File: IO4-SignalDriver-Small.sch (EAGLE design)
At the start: 17 parts, among them IC1 74HS139A

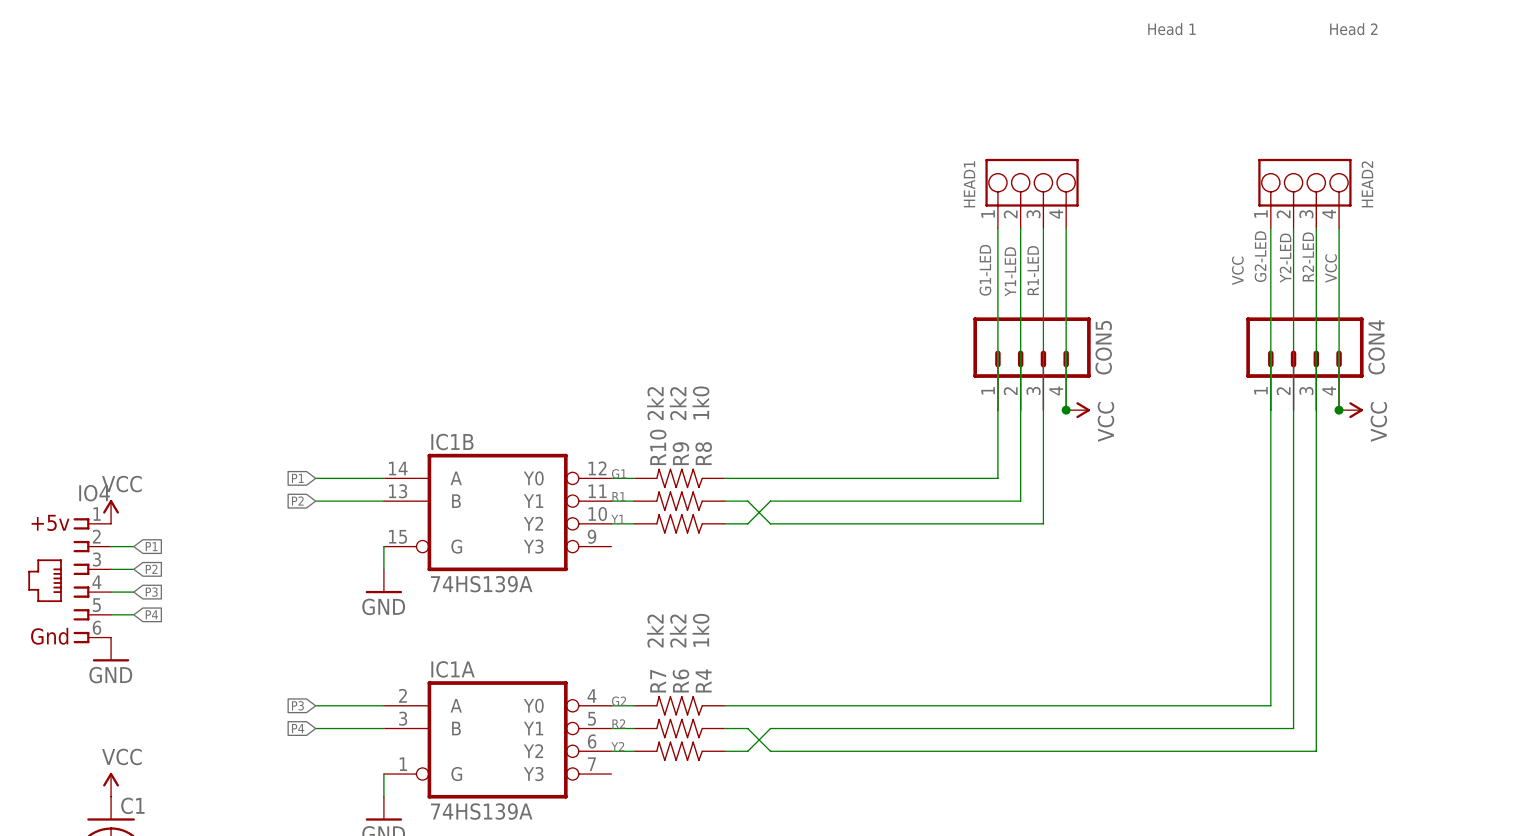
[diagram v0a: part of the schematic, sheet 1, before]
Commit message: added values for connectors
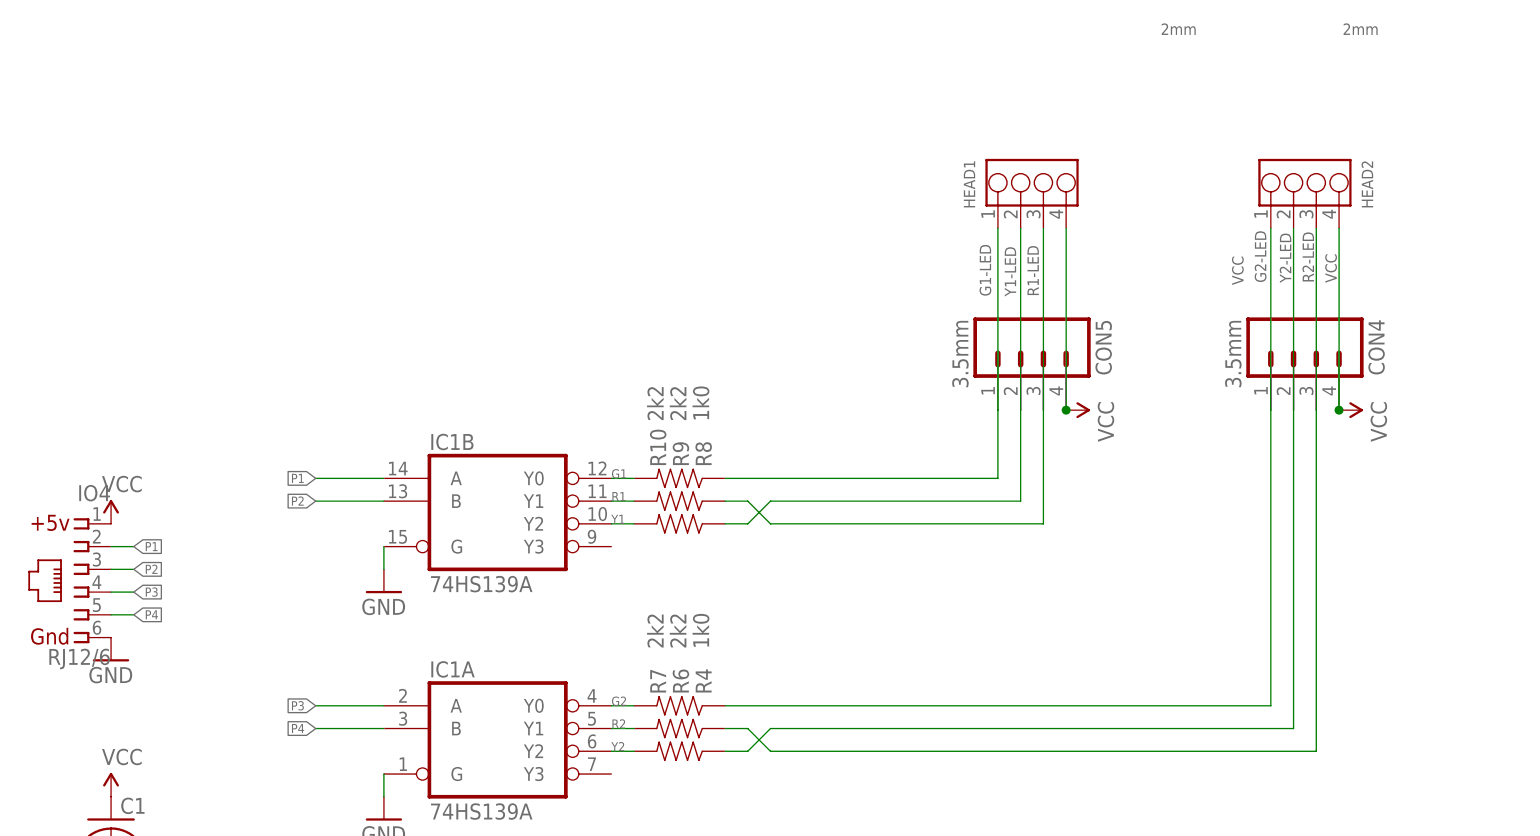
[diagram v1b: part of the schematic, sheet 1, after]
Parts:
- CON4, CON5: value (none) -> 3.5mm
- HEAD1: value Head 1 -> 2mm
- HEAD2: value Head 2 -> 2mm
- IO4: value (none) -> RJ12/6
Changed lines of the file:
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@@
 <grid distance="100" unitdist="mil" unit="mil" style="dots" multiple="1" display="yes" altdistance="50" altunitdist="mil" altunit="mil"/>
 <layers>
-<layer number="1" name="Top" color="4" fill="1" visible="yes" active="no"/>
-<layer number="2" name="Route2" color="1" fill="3" visible="yes" active="no"/>
-<layer number="3" name="Route3" color="4" fill="3" visible="yes" active="no"/>
-<layer number="14" name="Route14" color="1" fill="6" visible="yes" active="no"/>
-<layer number="15" name="Route15" color="4" fill="6" visible="yes" active="no"/>
-<layer number="16" name="Bottom" color="2" fill="1" visible="yes" active="no"/>
-<layer number="17" name="Pads" color="23" fill="1" visible="yes" active="no"/>
-<layer number="18" name="Vias" color="29" fill="1" visible="yes" active="no"/>
-<layer number="19" name="Unrouted" color="6" fill="1" visible="yes" active="no"/>
-<layer number="20" name="Dimension" color="15" fill="1" visible="yes" active="no"/>
-<layer number="21" name="tPlace" color="19" fill="1" visible="yes" active="no"/>
-<layer number="22" name="bPlace" color="17" fill="1" visible="yes" active="no"/>
-<layer number="23" name="tOrigins" color="30" fill="1" visible="yes" active="no"/>
-<layer number="24" name="bOrigins" color="15" fill="1" visible="yes" active="no"/>
-<layer number="25" name="tNames" color="63" fill="1" visible="yes" active="no"/>
-<layer number="26" name="bNames" color="34" fill="1" visible="yes" active="no"/>
-<layer number="27" name="tValues" color="56" fill="1" visible="yes" active="no"/>
-<layer number="28" name="bValues" color="7" fill="1" visible="yes" active="no"/>
+<layer number="1" name="Top" color="4" fill="1" visible="no" active="no"/>
+<layer number="2" name="Route2" color="1" fill="3" visible="no" active="no"/>
+<layer number="3" name="Route3" color="4" fill="3" visible="no" active="no"/>
+<layer number="14" name="Route14" color="1" fill="6" visible="no" active="no"/>
+<layer number="15" name="Route15" color="4" fill="6" visible="no" active="no"/>
+<layer number="16" name="Bottom" color="2" fill="1" visible="no" active="no"/>
+<layer number="17" name="Pads" color="23" fill="1" visible="no" active="no"/>
+<layer number="18" name="Vias" color="29" fill="1" visible="no" active="no"/>
+<layer number="19" name="Unrouted" color="6" fill="1" visible="no" active="no"/>
+<layer number="20" name="Dimension" color="15" fill="1" visible="no" active="no"/>
+<layer number="21" name="tPlace" color="19" fill="1" visible="no" active="no"/>
+<layer number="22" name="bPlace" color="17" fill="1" visible="no" active="no"/>
+<layer number="23" name="tOrigins" color="30" fill="1" visible="no" active="no"/>
+<layer number="24" name="bOrigins" color="15" fill="1" visible="no" active="no"/>
+<layer number="25" name="tNames" color="63" fill="1" visible="no" active="no"/>
+<layer number="26" name="bNames" color="34" fill="1" visible="no" active="no"/>
+<layer number="27" name="tValues" color="56" fill="1" visible="no" active="no"/>
+<layer number="28" name="bValues" color="7" fill="1" visible="no" active="no"/>
 <layer number="29" name="tStop" color="7" fill="3" visible="no" active="no"/>
 <layer number="30" name="bStop" color="7" fill="6" visible="no" active="no"/>
@@
 <layer number="35" name="tGlue" color="7" fill="4" visible="no" active="no"/>
 <layer number="36" name="bGlue" color="7" fill="5" visible="no" active="no"/>
-<layer number="37" name="tTest" color="7" fill="1" visible="yes" active="no"/>
-<layer number="38" name="bTest" color="7" fill="1" visible="yes" active="no"/>
+<layer number="37" name="tTest" color="7" fill="1" visible="no" active="no"/>
+<layer number="38" name="bTest" color="7" fill="1" visible="no" active="no"/>
 <layer number="39" name="tKeepout" color="4" fill="11" visible="no" active="no"/>
 <layer number="40" name="bKeepout" color="3" fill="11" visible="no" active="no"/>
@@
 <layer number="44" name="Drills" color="16" fill="1" visible="no" active="no"/>
 <layer number="45" name="Holes" color="35" fill="1" visible="no" active="no"/>
-<layer number="46" name="Milling" color="35" fill="1" visible="yes" active="no"/>
-<layer number="47" name="Measures" color="21" fill="1" visible="yes" active="no"/>
-<layer number="48" name="Document" color="15" fill="1" visible="yes" active="no"/>
-<layer number="49" name="Reference" color="48" fill="1" visible="yes" active="no"/>
-<layer number="50" name="dxf" color="7" fill="1" visible="yes" active="no"/>
-<layer number="51" name="tDocu" color="24" fill="1" visible="yes" active="no"/>
-<layer number="52" name="bDocu" color="7" fill="1" visible="yes" active="no"/>
-<layer number="53" name="tGND_GNDA" color="7" fill="9" visible="yes" active="no"/>
-<layer number="54" name="bGND_GNDA" color="1" fill="9" visible="yes" active="no"/>
-<layer number="56" name="wert" color="7" fill="1" visible="yes" active="no"/>
-<layer number="57" name="tCAD" color="7" fill="1" visible="yes" active="no"/>
-<layer number="59" name="tCarbon" color="7" fill="1" visible="yes" active="no"/>
-<layer number="60" name="bCarbon" color="7" fill="1" visible="yes" active="no"/>
+<layer number="46" name="Milling" color="35" fill="1" visible="no" active="no"/>
+<layer number="47" name="Measures" color="21" fill="1" visible="no" active="no"/>
+<layer number="48" name="Document" color="15" fill="1" visible="no" active="no"/>
+<layer number="49" name="Reference" color="48" fill="1" visible="no" active="no"/>
+<layer number="50" name="dxf" color="7" fill="1" visible="no" active="no"/>
+<layer number="51" name="tDocu" color="24" fill="1" visible="no" active="no"/>
+<layer number="52" name="bDocu" color="7" fill="1" visible="no" active="no"/>
+<layer number="53" name="tGND_GNDA" color="7" fill="9" visible="no" active="no"/>
+<layer number="54" name="bGND_GNDA" color="1" fill="9" visible="no" active="no"/>
+<layer number="56" name="wert" color="7" fill="1" visible="no" active="no"/>
+<layer number="57" name="tCAD" color="7" fill="1" visible="no" active="no"/>
+<layer number="59" name="tCarbon" color="7" fill="1" visible="no" active="no"/>
+<layer number="60" name="bCarbon" color="7" fill="1" visible="no" active="no"/>
 <layer number="90" name="Modules" color="5" fill="1" visible="yes" active="yes"/>
 <layer number="91" name="Nets" color="2" fill="1" visible="yes" active="yes"/>
@@
 <part name="R9" library="SPCoast" deviceset="R*" device="0805-RES" value="2k2"/>
 <part name="R10" library="SPCoast" deviceset="R*" device="0805-RES" value="2k2"/>
-<part name="IO4" library="SPCoast" deviceset="CONNECTOR-IO4" device="INV"/>
+<part name="IO4" library="SPCoast" deviceset="CONNECTOR-IO4" device="INV" value="RJ12/6"/>
 <part name="P+3" library="SparkFun" deviceset="VCC" device=""/>
 <part name="GND4" library="SparkFun" deviceset="GND" device=""/>
 <part name="FRAME2" library="SPCoast" deviceset="DOC-FRAME-LETTER" device=""/>
-<part name="CON4" library="SPCoast" deviceset="CONNECTOR-M04" device="SCREW"/>
-<part name="CON5" library="SPCoast" deviceset="CONNECTOR-M04" device="SCREW"/>
+<part name="CON4" library="SPCoast" deviceset="CONNECTOR-M04" device="SCREW" value="3.5mm"/>
+<part name="CON5" library="SPCoast" deviceset="CONNECTOR-M04" device="SCREW" value="3.5mm"/>
 <part name="P+7" library="SparkFun" deviceset="VCC" device=""/>
 <part name="P+9" library="SparkFun" deviceset="VCC" device=""/>
-<part name="HEAD1" library="SPCoast" deviceset="CONNECTOR-GROVE-4P-2.0" device="-3470130P1" value="Head 1"/>
-<part name="HEAD2" library="SPCoast" deviceset="CONNECTOR-GROVE-4P-2.0" device="-3470130P1" value="Head 2"/>
+<part name="HEAD1" library="SPCoast" deviceset="CONNECTOR-GROVE-4P-2.0" device="-3470130P1" value="2mm"/>
+<part name="HEAD2" library="SPCoast" deviceset="CONNECTOR-GROVE-4P-2.0" device="-3470130P1" value="2mm"/>
 <part name="U$1" library="SPCoast" deviceset="MOUNTINGHOLE" device=""/>
 <part name="U$2" library="SPCoast" deviceset="MOUNTINGHOLE" device=""/>

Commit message: normalized values
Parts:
- C1: device SPCoast:CAP0805 -> SPCoast:CAP0603
- R10, R4, R6, R7, R8, R9: device SPCoast:R0805-RES -> SPCoast:R0603-RES
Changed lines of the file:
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@@
 <grid distance="100" unitdist="mil" unit="mil" style="dots" multiple="1" display="yes" altdistance="50" altunitdist="mil" altunit="mil"/>
 <layers>
-<layer number="1" name="Top" color="4" fill="1" visible="no" active="no"/>
-<layer number="2" name="Route2" color="1" fill="3" visible="no" active="no"/>
-<layer number="3" name="Route3" color="4" fill="3" visible="no" active="no"/>
-<layer number="14" name="Route14" color="1" fill="6" visible="no" active="no"/>
-<layer number="15" name="Route15" color="4" fill="6" visible="no" active="no"/>
-<layer number="16" name="Bottom" color="2" fill="1" visible="no" active="no"/>
-<layer number="17" name="Pads" color="23" fill="1" visible="no" active="no"/>
-<layer number="18" name="Vias" color="29" fill="1" visible="no" active="no"/>
-<layer number="19" name="Unrouted" color="6" fill="1" visible="no" active="no"/>
-<layer number="20" name="Dimension" color="15" fill="1" visible="no" active="no"/>
-<layer number="21" name="tPlace" color="19" fill="1" visible="no" active="no"/>
-<layer number="22" name="bPlace" color="17" fill="1" visible="no" active="no"/>
-<layer number="23" name="tOrigins" color="30" fill="1" visible="no" active="no"/>
-<layer number="24" name="bOrigins" color="15" fill="1" visible="no" active="no"/>
-<layer number="25" name="tNames" color="63" fill="1" visible="no" active="no"/>
-<layer number="26" name="bNames" color="34" fill="1" visible="no" active="no"/>
-<layer number="27" name="tValues" color="56" fill="1" visible="no" active="no"/>
-<layer number="28" name="bValues" color="7" fill="1" visible="no" active="no"/>
+<layer number="1" name="Top" color="4" fill="1" visible="yes" active="no"/>
+<layer number="2" name="Route2" color="1" fill="3" visible="yes" active="no"/>
+<layer number="3" name="Route3" color="4" fill="3" visible="yes" active="no"/>
+<layer number="14" name="Route14" color="1" fill="6" visible="yes" active="no"/>
+<layer number="15" name="Route15" color="4" fill="6" visible="yes" active="no"/>
+<layer number="16" name="Bottom" color="2" fill="1" visible="yes" active="no"/>
+<layer number="17" name="Pads" color="23" fill="1" visible="yes" active="no"/>
+<layer number="18" name="Vias" color="29" fill="1" visible="yes" active="no"/>
+<layer number="19" name="Unrouted" color="6" fill="1" visible="yes" active="no"/>
+<layer number="20" name="Dimension" color="15" fill="1" visible="yes" active="no"/>
+<layer number="21" name="tPlace" color="19" fill="1" visible="yes" active="no"/>
+<layer number="22" name="bPlace" color="17" fill="1" visible="yes" active="no"/>
+<layer number="23" name="tOrigins" color="30" fill="1" visible="yes" active="no"/>
+<layer number="24" name="bOrigins" color="15" fill="1" visible="yes" active="no"/>
+<layer number="25" name="tNames" color="63" fill="1" visible="yes" active="no"/>
+<layer number="26" name="bNames" color="34" fill="1" visible="yes" active="no"/>
+<layer number="27" name="tValues" color="56" fill="1" visible="yes" active="no"/>
+<layer number="28" name="bValues" color="7" fill="1" visible="yes" active="no"/>
 <layer number="29" name="tStop" color="7" fill="3" visible="no" active="no"/>
 <layer number="30" name="bStop" color="7" fill="6" visible="no" active="no"/>
@@
 <layer number="35" name="tGlue" color="7" fill="4" visible="no" active="no"/>
 <layer number="36" name="bGlue" color="7" fill="5" visible="no" active="no"/>
-<layer number="37" name="tTest" color="7" fill="1" visible="no" active="no"/>
-<layer number="38" name="bTest" color="7" fill="1" visible="no" active="no"/>
+<layer number="37" name="tTest" color="7" fill="1" visible="yes" active="no"/>
+<layer number="38" name="bTest" color="7" fill="1" visible="yes" active="no"/>
 <layer number="39" name="tKeepout" color="4" fill="11" visible="no" active="no"/>
 <layer number="40" name="bKeepout" color="3" fill="11" visible="no" active="no"/>
@@
 <layer number="44" name="Drills" color="16" fill="1" visible="no" active="no"/>
 <layer number="45" name="Holes" color="35" fill="1" visible="no" active="no"/>
-<layer number="46" name="Milling" color="35" fill="1" visible="no" active="no"/>
-<layer number="47" name="Measures" color="21" fill="1" visible="no" active="no"/>
-<layer number="48" name="Document" color="15" fill="1" visible="no" active="no"/>
-<layer number="49" name="Reference" color="48" fill="1" visible="no" active="no"/>
-<layer number="50" name="dxf" color="7" fill="1" visible="no" active="no"/>
-<layer number="51" name="tDocu" color="24" fill="1" visible="no" active="no"/>
-<layer number="52" name="bDocu" color="7" fill="1" visible="no" active="no"/>
-<layer number="53" name="tGND_GNDA" color="7" fill="9" visible="no" active="no"/>
-<layer number="54" name="bGND_GNDA" color="1" fill="9" visible="no" active="no"/>
-<layer number="56" name="wert" color="7" fill="1" visible="no" active="no"/>
-<layer number="57" name="tCAD" color="7" fill="1" visible="no" active="no"/>
-<layer number="59" name="tCarbon" color="7" fill="1" visible="no" active="no"/>
-<layer number="60" name="bCarbon" color="7" fill="1" visible="no" active="no"/>
+<layer number="46" name="Milling" color="35" fill="1" visible="yes" active="no"/>
+<layer number="47" name="Measures" color="21" fill="1" visible="yes" active="no"/>
+<layer number="48" name="Document" color="15" fill="1" visible="yes" active="no"/>
+<layer number="49" name="Reference" color="48" fill="1" visible="yes" active="no"/>
+<layer number="50" name="dxf" color="7" fill="1" visible="yes" active="no"/>
+<layer number="51" name="tDocu" color="24" fill="1" visible="yes" active="no"/>
+<layer number="52" name="bDocu" color="7" fill="1" visible="yes" active="no"/>
+<layer number="53" name="tGND_GNDA" color="7" fill="9" visible="yes" active="no"/>
+<layer number="54" name="bGND_GNDA" color="1" fill="9" visible="yes" active="no"/>
+<layer number="56" name="wert" color="7" fill="1" visible="yes" active="no"/>
+<layer number="57" name="tCAD" color="7" fill="1" visible="yes" active="no"/>
+<layer number="59" name="tCarbon" color="7" fill="1" visible="yes" active="no"/>
+<layer number="60" name="bCarbon" color="7" fill="1" visible="yes" active="no"/>
 <layer number="90" name="Modules" color="5" fill="1" visible="yes" active="yes"/>
 <layer number="91" name="Nets" color="2" fill="1" visible="yes" active="yes"/>
@@
 <part name="FID1" library="SPCoast" deviceset="FIDUCIAL" device=""/>
 <part name="IC1" library="SPCoast" deviceset="74*139" device="D" technology="LS" value="74HS139A"/>
-<part name="C1" library="SPCoast" deviceset="CAP*" device="0805" value="0.1UF"/>
+<part name="C1" library="SPCoast" deviceset="CAP*" device="0603" value="0.1UF"/>
 <part name="P+2" library="SparkFun" deviceset="VCC" device=""/>
 <part name="GND1" library="SparkFun" deviceset="GND" device=""/>
 <part name="GND2" library="SparkFun" deviceset="GND" device=""/>
 <part name="GND3" library="SparkFun" deviceset="GND" device=""/>
-<part name="R4" library="SPCoast" deviceset="R*" device="0805-RES" value="1k0"/>
-<part name="R6" library="SPCoast" deviceset="R*" device="0805-RES" value="2k2"/>
-<part name="R7" library="SPCoast" deviceset="R*" device="0805-RES" value="2k2"/>
-<part name="R8" library="SPCoast" deviceset="R*" device="0805-RES" value="1k0"/>
-<part name="R9" library="SPCoast" deviceset="R*" device="0805-RES" value="2k2"/>
-<part name="R10" library="SPCoast" deviceset="R*" device="0805-RES" value="2k2"/>
+<part name="R4" library="SPCoast" deviceset="R*" device="0603-RES" value="1k0"/>
+<part name="R6" library="SPCoast" deviceset="R*" device="0603-RES" value="2k2"/>
+<part name="R7" library="SPCoast" deviceset="R*" device="0603-RES" value="2k2"/>
+<part name="R8" library="SPCoast" deviceset="R*" device="0603-RES" value="1k0"/>
+<part name="R9" library="SPCoast" deviceset="R*" device="0603-RES" value="2k2"/>
+<part name="R10" library="SPCoast" deviceset="R*" device="0603-RES" value="2k2"/>
 <part name="IO4" library="SPCoast" deviceset="CONNECTOR-IO4" device="INV" value="RJ12/6"/>
 <part name="P+3" library="SparkFun" deviceset="VCC" device=""/>
